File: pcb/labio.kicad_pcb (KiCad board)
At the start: 2 copper layers, 152 x 85 mm, 219 parts, among them IC201 AT24CS32-XHM, J701 JACK_TRRS_6PINS, P1 CONN_02X20, P301 CONN_01X04, P302 CONN_01X04, P303 CONN_01X04, P401 SFV12R-1ST__HLF, P601 CONN_01X02, P602 CONN_01X02, P603 CONN_01X04, P604 CONN_01X02, P605 CONN_01X03, P606 CONN_01X03, P607 CONN_01X05, P608 CONN_01X05, P701 CONN_01X04, P702 CONN_01X04, P703 CONN_01X04, P704 CONN_01X02, P901 CONN_01X06, Q301 PHOTOTRANSISTOR, Q302 Q_NMOS_GSD, Q303 Q_NMOS_GSD, Q601 Q_NMOS_GSD, Q602 Q_NMOS_GSD, Q603 Q_NMOS_GSD, Q604 Q_NMOS_GSD, Q605 Q_NMOS_GSD, Q606 Q_NMOS_GSD, Q607 Q_NMOS_GSD, Q608 Q_NMOS_GSD, Q609 Q_NMOS_GSD, Q610 Q_NMOS_GSD, Q611 Q_NMOS_GSD, Q612 Q_NMOS_GSD, Q613 Q_NMOS_GSD, SW301 DIP_SWITCH_X04, SW401 DIP_SWITCH_X04, SW501 DIP_SWITCH_X04, SW601 DIP_SWITCH_X04, SW602 DIP_SWITCH_X04, SW603 DIP_SWITCH_X04, SW604 DIP_SWITCH_X04, SW605 ROT_ENC, SW606 DIP_SWITCH_X04, SW701 DIP_SWITCH_X04, SW702 DIP_SWITCH_X04, SW801 SW_PUSH, SW802 SW_PUSH, SW803 SW_PUSH, SW804 SW_PUSH, SW805 SW_PUSH, U201 AP7365_SOT-23-5, U301 ADS1015, U501 LSM303D, U502 BMP280, U503 L3GD20H, U601 L298P_PowerSO20, U701 SPU0410HR5H, U702 WM8731

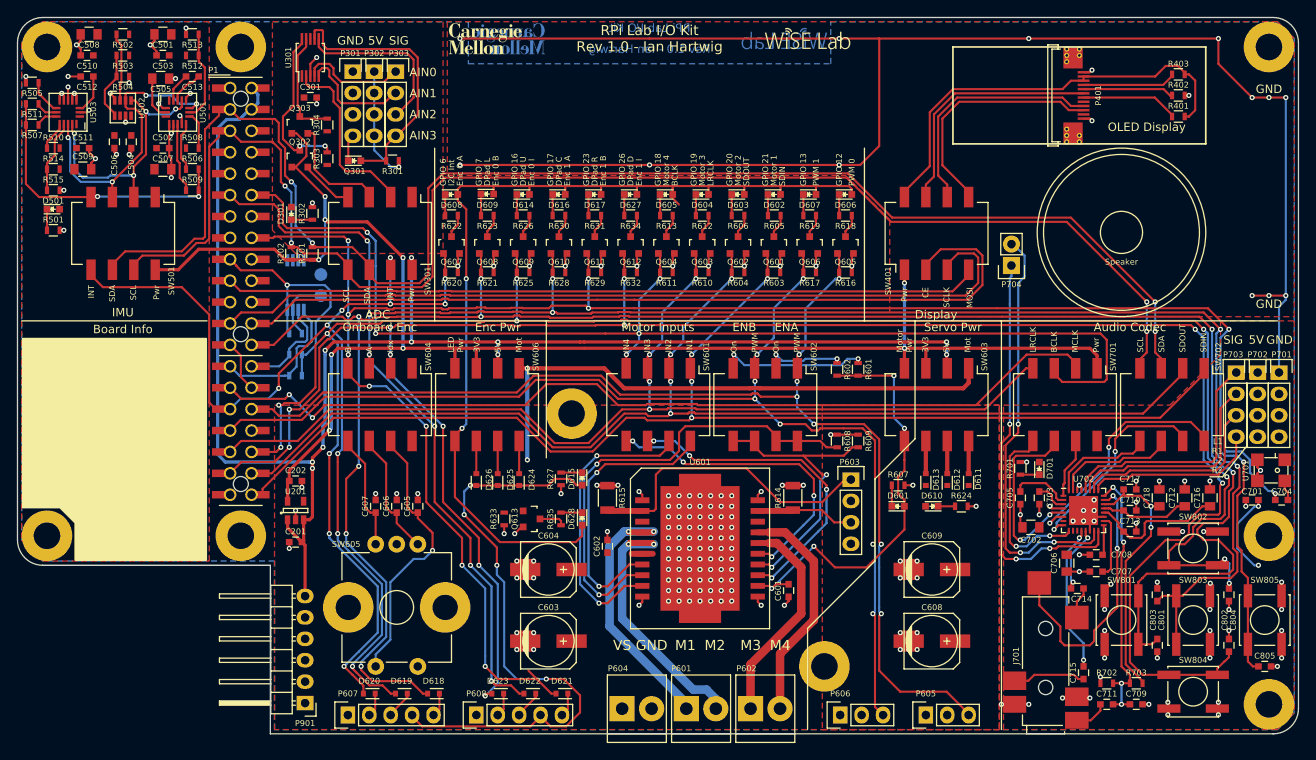
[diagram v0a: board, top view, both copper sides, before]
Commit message: Fix board/bom errors from initial build
* Accelerometer (U501) footprint mirrored. Redraw footprint and adjust routing.
* Gyro (U505) footprint mirrored. Redraw footprint and adjust routing.
* Codec (U702) labed as wrong chip. Says WM8731 but should be 8750. Also fix in BOM.
* Should include OLED screen in BOM (not just the connector).
* Codec to TRRS caps have incorrect value. Says 220uF but should be 220pF.
* Mark RPi Hat EEPROM circuit as depopulated in schematic.
* Remove dangling trace near encoder headers.
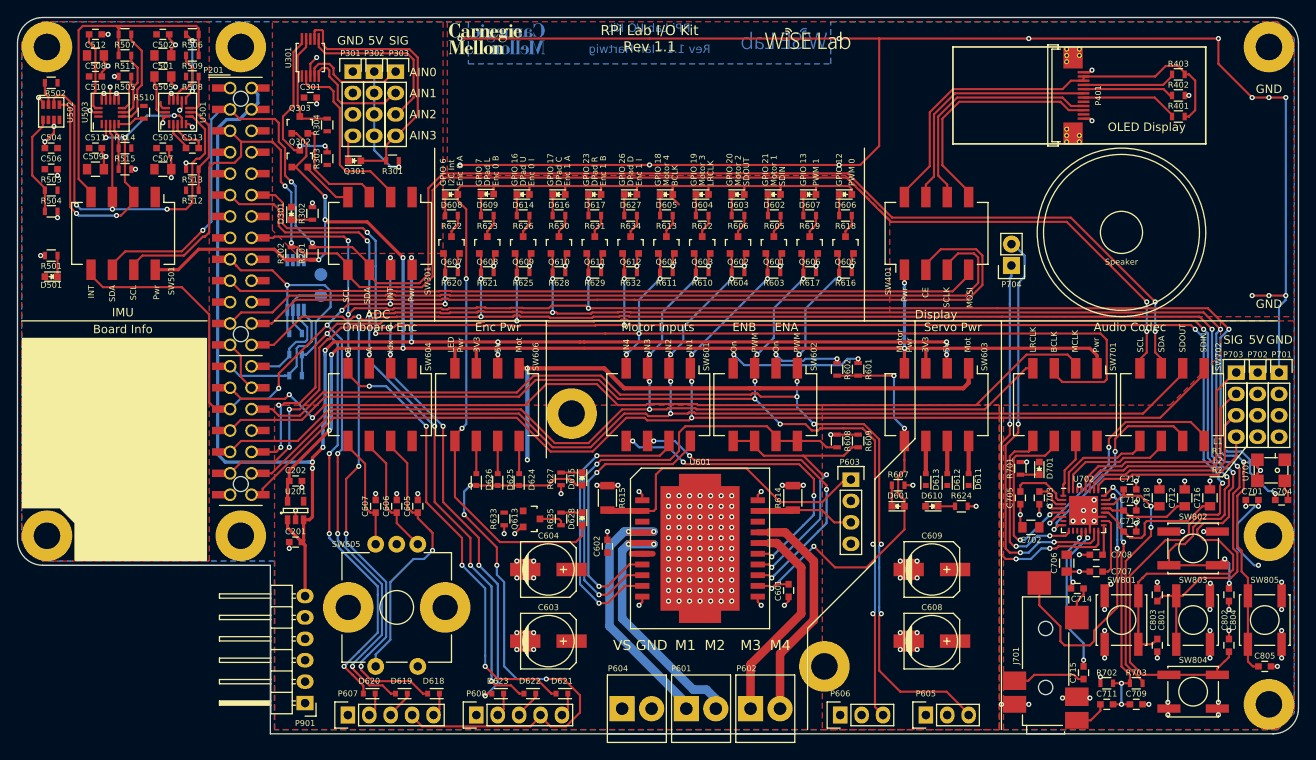
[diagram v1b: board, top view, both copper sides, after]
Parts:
- C714, C715: value 220uF -> 220pF
- IC201: value AT24CS32-XHM -> dnp-AT24CS32-XHM
- R203: value 10k -> dnp-10k
- R204, R205: value 3.9k -> dnp-3.9k
- R302, R501, R605, R606, R607, R612, R613, R618, R619, R622, R623, R624, R626, R627, R630, R631, R634, R635, R701: value 2k -> 220
- U702: value WM8731 -> WM8750
- moved R503 18.1 mm to (81.0, 70.5)
- moved R504 18.1 mm to (81.0, 73.0)
- moved R506 16.0 mm to (97.8, 52.0)
- moved R509 16.0 mm to (97.8, 54.5)
- moved R512 16.0 mm to (97.8, 70.5)
- moved R513 16.0 mm to (97.8, 68.0)
- moved R507 15.4 mm to (89.8, 52.0)
- moved C502 13.5 mm to (94.2, 52.0)
- moved R511 12.4 mm to (89.8, 54.5)
- moved R510 11.6 mm to (92.0, 61.2), turned to 270 degrees
- moved R505 11.0 mm to (89.8, 57.0)
- moved C503 11.0 mm to (94.2, 65.5), turned to 0 degrees
- moved R502 10.3 mm to (81.0, 57.8)
- moved C504 9.53 mm to (81.0, 65.5), turned to 180 degrees
- moved R514 8.86 mm to (89.8, 65.5)
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- renumbered P1 to P201
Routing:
- net /labio-imu/SDA_J: track 36.3 -> 52.3 mm, vias 4 -> 3
- net /labio-imu/SCL_J: track 31.6 -> 42.5 mm, vias 4 -> 5
- net /labio-imu/GYRO_INT2: track 2.63 -> 11.9 mm
- net /labio-imu/INT_J: track 33.9 -> 42.2 mm, vias 2 -> 0
- net /labio-imu/GYRO_INT1: track 2.63 -> 8.27 mm
- net /labio-imu/BMP_CS: track 8.15 -> 2.78 mm
- net Net-(C512-Pad1): track 4.62 -> 9.62 mm
- net /labio-imu/BMP_ADDR: track 8.20 -> 12.0 mm
- net /labio-imu/GYRO_SA0: track 8.68 -> 5.56 mm
- net /labio-imu/ACCEL_INT2: track 5.83 -> 8.47 mm, vias 0 -> 2
- net /labio-imu/ACCEL_INT1: track 8.30 -> 6.68 mm
- net /labio-dpad/DPAD_RIGHT: track 239.2 -> 237.8 mm
- net /labio-imu/VDD3V3_J: track 0.00 -> 1.20 mm
- net GND: track 507.3 -> 506.3 mm
- net /labio-rpi/GPIO3_SCL1: track 174.4 -> 175.2 mm
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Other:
- board text added: "RPi Lab I/O Kit Rev 1.1"
- board text added: "Rev 1.1 - Ian Hartwig"
- board text removed: "RPi Lab I/O Kit Rev 1.0 - Ian Hartwig"
- board text removed: "Rev 1.0 - Ian Hartwig"

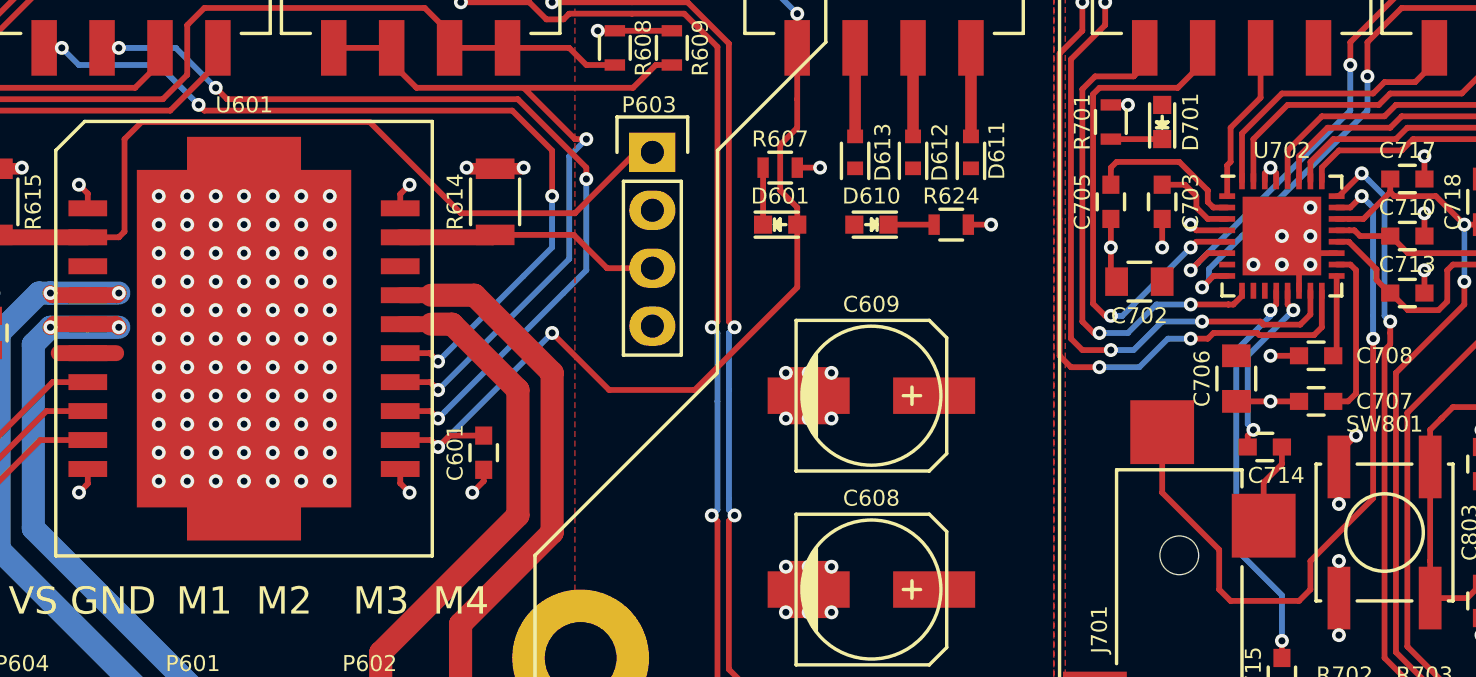
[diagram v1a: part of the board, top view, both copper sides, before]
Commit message: Use soldermask windows on footprints with thermal pads (motor driver, codec)
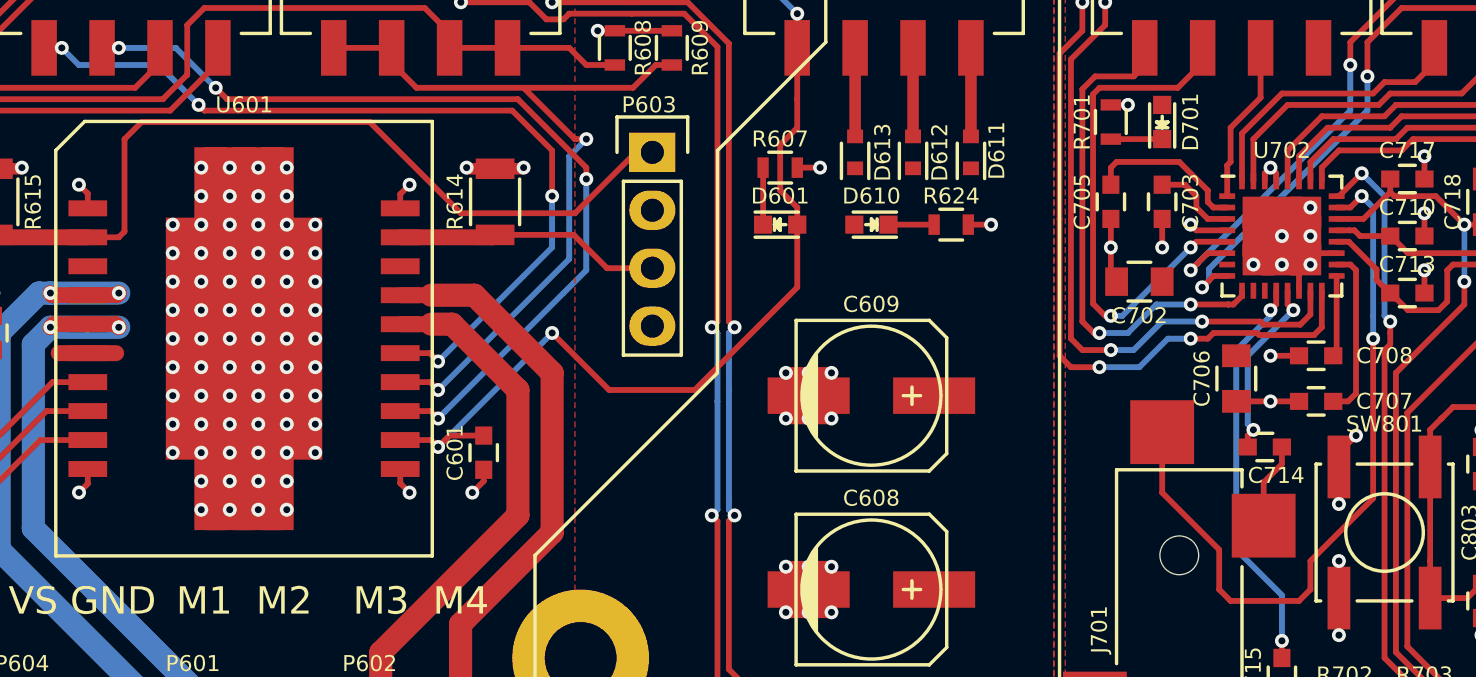
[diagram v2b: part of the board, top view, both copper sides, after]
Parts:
- U702: footprint Housings_DFN_QFN:QFN-32-1EP_5x5mm_Pitch0.5mm -> labio-special:QFN-32-1EP_5x5mm_Pitch0.5mm
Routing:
- net GND: track 506.3 -> 408.9 mm, vias 225 -> 218

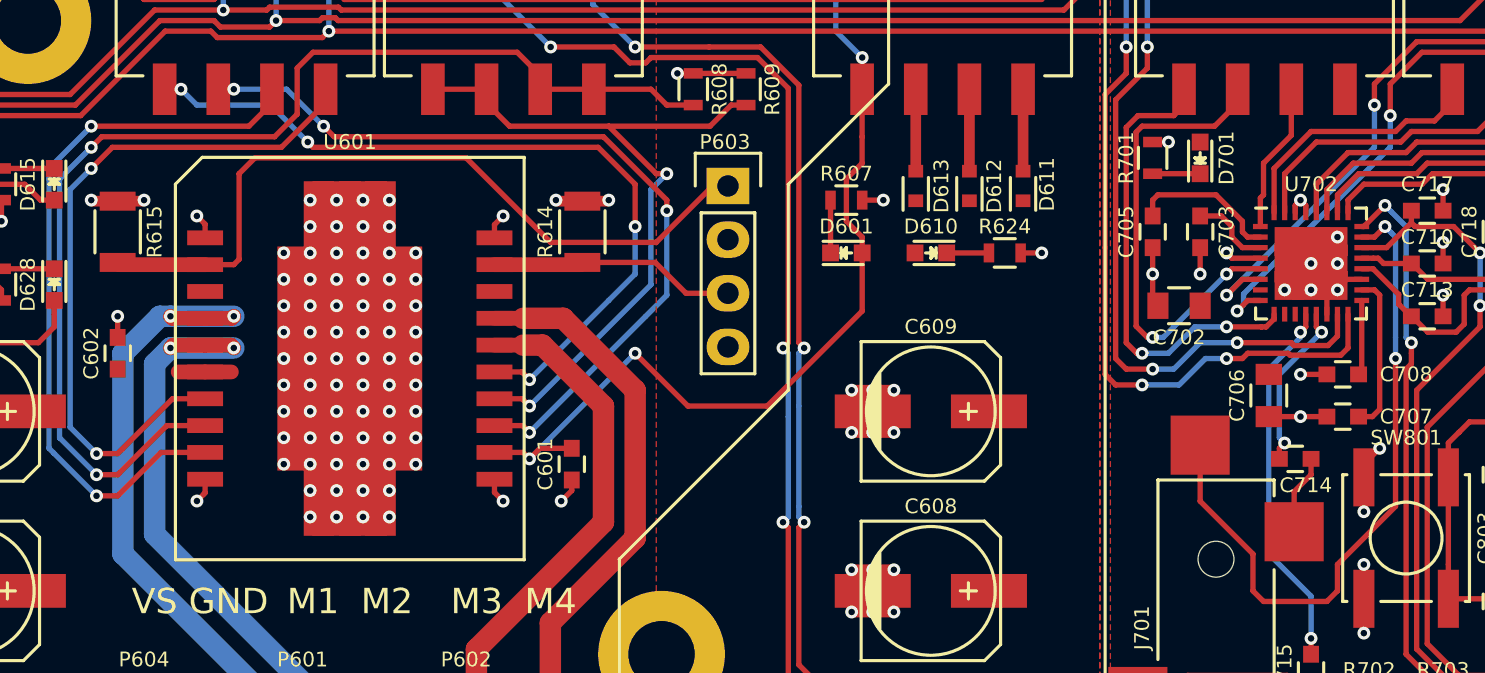
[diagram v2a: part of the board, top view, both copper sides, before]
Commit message: improve codec and motor driver soldermask windows to avoid convex 90 deg angles
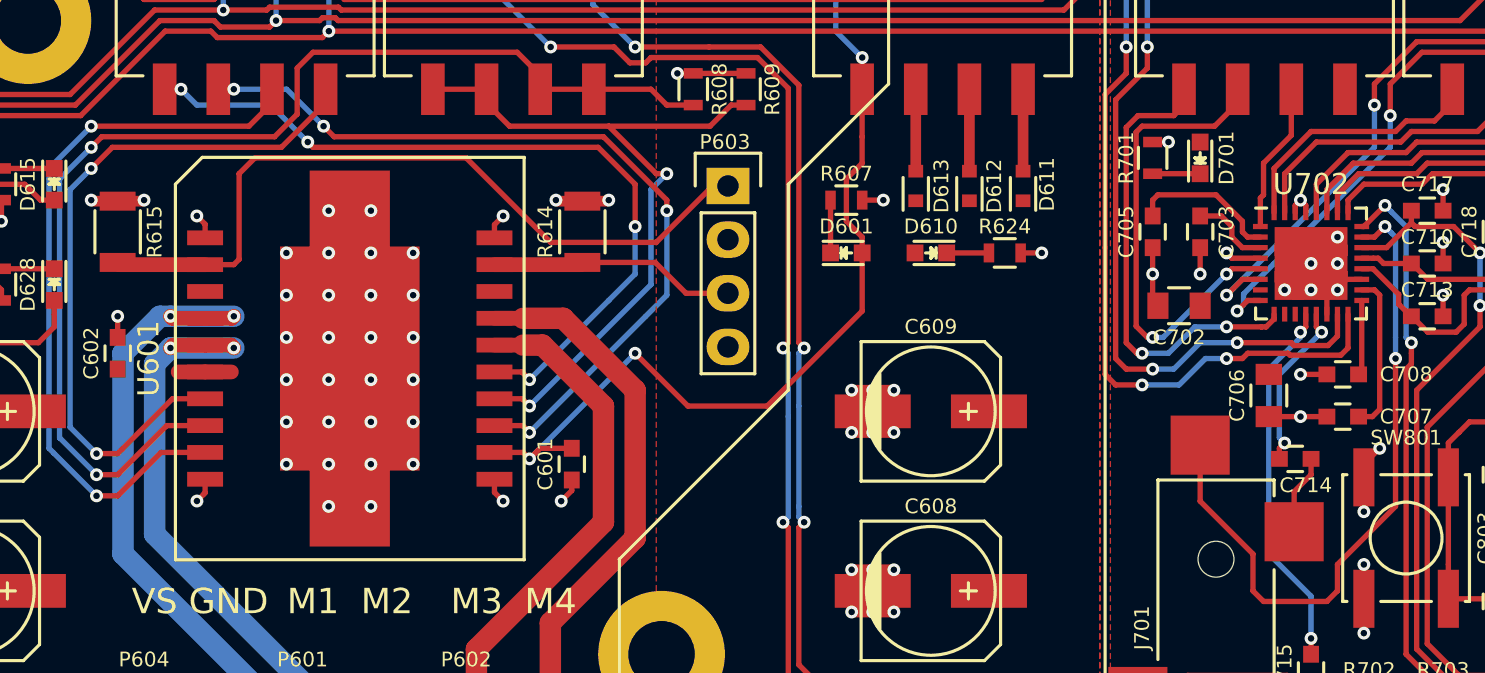
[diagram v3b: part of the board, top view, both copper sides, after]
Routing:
- net GND: vias 218 -> 176

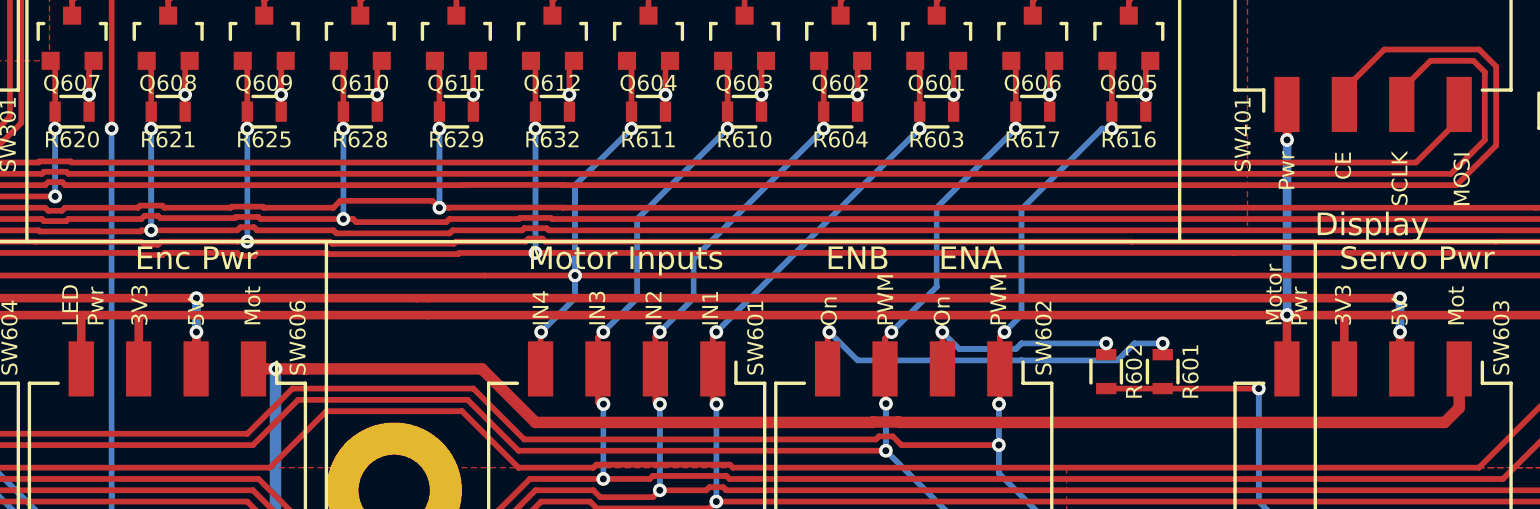
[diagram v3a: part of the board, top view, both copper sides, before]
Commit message: Power motor driver from 5V but with 3.3V logic. Adjust R601, R602 to prevent more than 3.3V on logic lines.
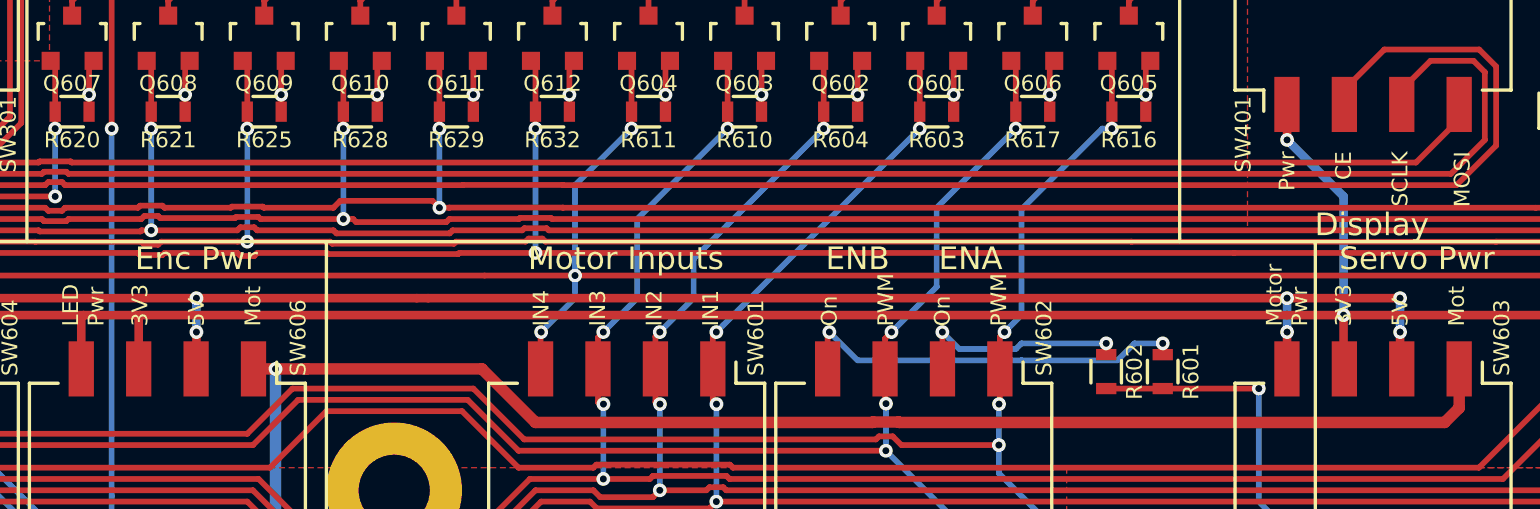
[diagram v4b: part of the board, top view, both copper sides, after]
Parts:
- R601, R602: value 1k -> 10k
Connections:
- net /labio-adc/ALERT renamed /I2C_INT
- net /labio-audio/BCLK renamed /I2S_BCLK
- net /labio-rpi/GPIO12_PWM0 renamed /PWM0
- net /labio-rpi/GPIO13_PWM1 renamed /PWM1
- net /labio-rpi/GPIO19_PCM_FS renamed /I2S_LRCLK
- net /labio-rpi/GPIO1_SDA1 renamed /I2C_SDA
- net /labio-rpi/GPIO20_PCM_DIN renamed /I2S_SDOUT
- net /labio-rpi/GPIO21_PCM_DOUT renamed /I2S_SDIN
- net /labio-rpi/GPIO3_SCL1 renamed /I2C_SCL
- net /labio-rpi/GPIO5 renamed /GPCLK1
- C201 pad 1: /labio-rpi/VBUS -> /5V
- C202 pad 1: /labio-rpi/3V3_EXTRA -> /3V3_EXTRA
- H1001 pad 1: (no net) -> Net-(H1001-Pad1)
- H1002 pad 1: (no net) -> Net-(H1002-Pad1)
- H1003 pad 1: (no net) -> Net-(H1003-Pad1)
- H1004 pad 1: (no net) -> Net-(H1004-Pad1)
- H1005 pad 1: (no net) -> Net-(H1005-Pad1)
- H1006 pad 1: (no net) -> Net-(H1006-Pad1)
- H1007 pad 1: (no net) -> Net-(H1007-Pad1)
- H1008 pad 1: (no net) -> Net-(H1008-Pad1)
- H1009 pad 1: (no net) -> Net-(H1009-Pad1)
- J701 pad 6: (no net) -> Net-(J701-Pad6)
- P201 pad 2: /labio-rpi/VBUS -> /5V
- P201 pad 4: /labio-rpi/VBUS -> /5V
- P401 pad 11: (no net) -> Net-(P401-Pad11)
- P401 pad 8: (no net) -> Net-(P401-Pad8)
- P901 pad 5: (no net) -> Net-(P901-Pad5)
- P901 pad 6: /labio-rpi/VBUS -> /5V
- Q302 pad 1: /labio-rpi/3V3_EXTRA -> /3V3_EXTRA
- Q303 pad 1: /labio-rpi/3V3_EXTRA -> /3V3_EXTRA
- R201 pad 1: /labio-rpi/3V3_EXTRA -> /3V3_EXTRA
- R202 pad 1: /labio-rpi/3V3_EXTRA -> /3V3_EXTRA
- SW301 pad 8: /labio-rpi/VBUS -> /5V
- SW401 pad 1: /labio-rpi/3V3_EXTRA -> /3V3_EXTRA
- SW501 pad 8: /labio-rpi/3V3_EXTRA -> /3V3_EXTRA
- SW603 pad 2: /labio-rpi/VBUS -> /5V
- SW603 pad 3: /labio-rpi/3V3_EXTRA -> /3V3_EXTRA
- SW603 pad 4: /labio-rpi/3V3_EXTRA -> /5V
- SW604 pad 1: (no net) -> Net-(SW604-Pad1)
- SW604 pad 8: (no net) -> Net-(SW604-Pad8)
- SW606 pad 2: /labio-rpi/VBUS -> /5V
- SW606 pad 3: /labio-rpi/3V3_EXTRA -> /3V3_EXTRA
- SW606 pad 4: /labio-rpi/3V3_EXTRA -> /3V3_EXTRA
- SW701 pad 1: /labio-rpi/3V3_EXTRA -> /3V3_EXTRA
- U201 pad 1: /labio-rpi/VBUS -> /5V
- U201 pad 3: /labio-rpi/VBUS -> /5V
- U201 pad 5: /labio-rpi/3V3_EXTRA -> /3V3_EXTRA
- U702 pad 10: (no net) -> Net-(U702-Pad10)
- U702 pad 11: (no net) -> Net-(U702-Pad11)
- U702 pad 7: (no net) -> Net-(U702-Pad7)
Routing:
- net /labio-rpi/3V3_EXTRA: track 193.1 -> 0.00 mm, vias 9 -> 0
- net /3V3_EXTRA: track 0.00 -> 191.8 mm, vias 0 -> 9
- net /5V: track 0.00 -> 191.1 mm, vias 0 -> 12
- net /labio-rpi/VBUS: track 187.9 -> 0.00 mm, vias 10 -> 0
- net Net-(J701-Pad6): track 0.00 -> 3.25 mm, vias 0 -> 2
- net (no net): track 3.25 -> 0.00 mm, vias 2 -> 0
